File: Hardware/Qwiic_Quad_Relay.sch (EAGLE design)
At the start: 69 parts, among them J2 Qwiic Right Angle, J3 Qwiic Right Angle, J4 POWER_JACK, J9 AVR_SPI_PROG_3X2TESTPOINTS, K1 RELAY-SPDT-JZC-11F, K2 RELAY-SPDT-JZC-11F, K3 RELAY-SPDT-JZC-11F, K4 RELAY-SPDT-JZC-11F, Q1 600mA/40V, Q2 600mA/40V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

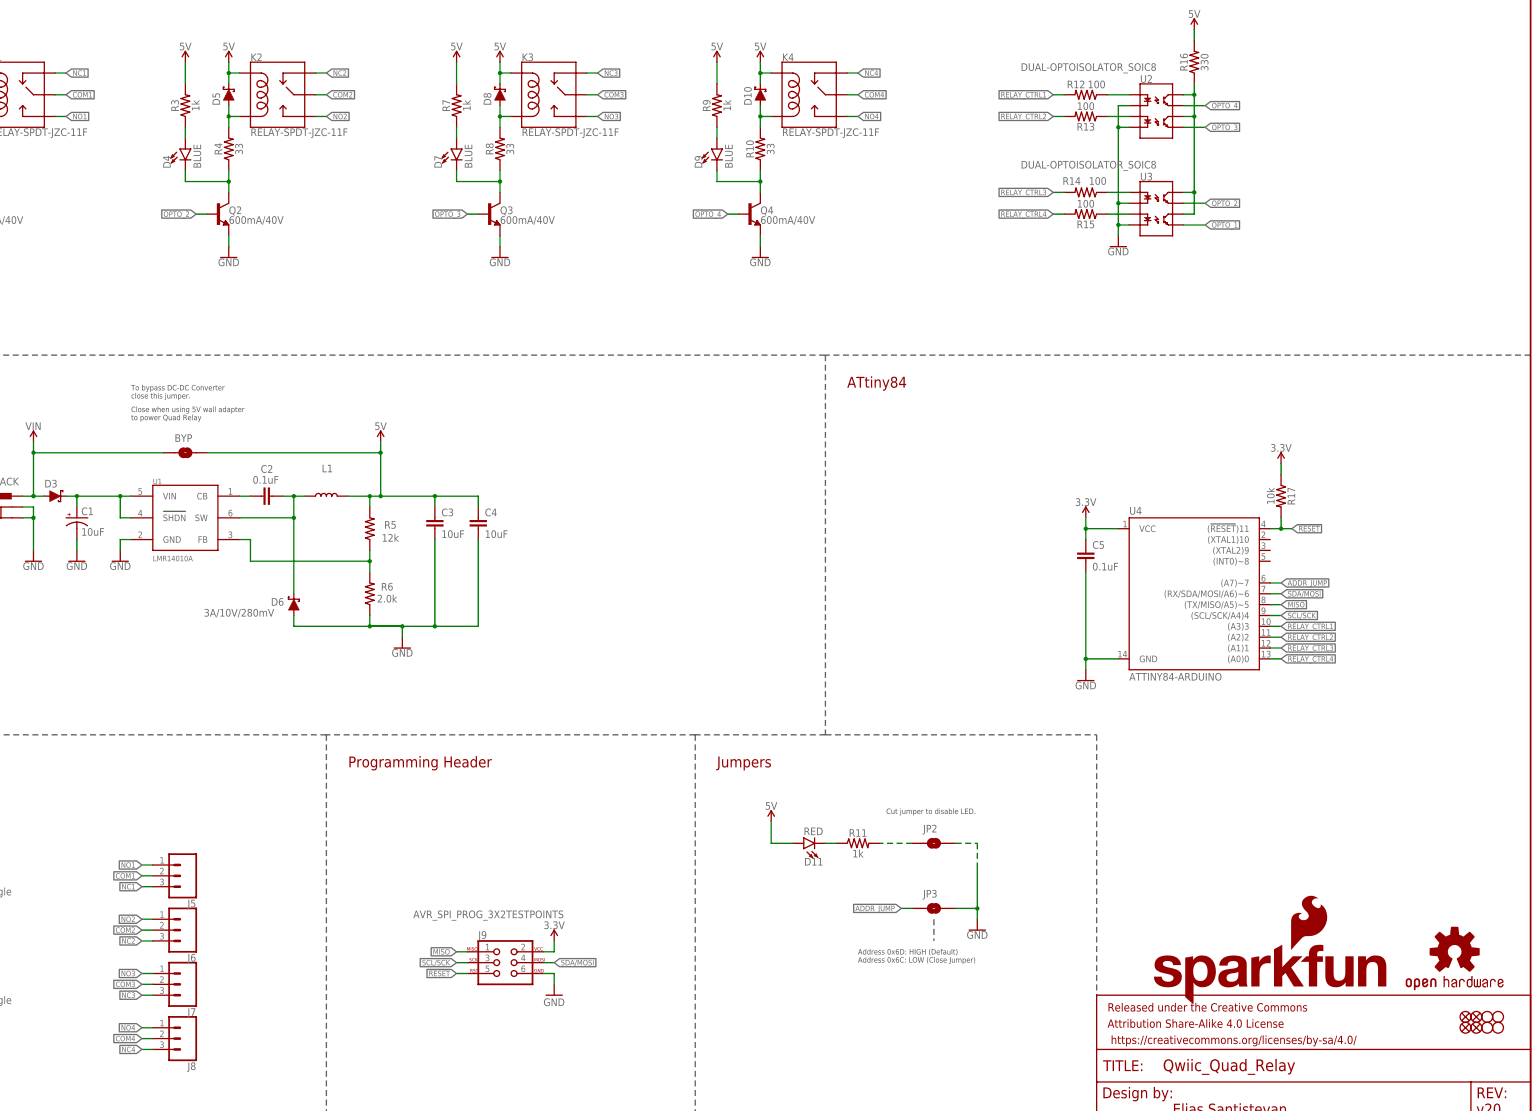
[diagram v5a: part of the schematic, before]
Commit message: Adds better silk, additional standoff, schotkky diode to protect dc/dc converter circuit
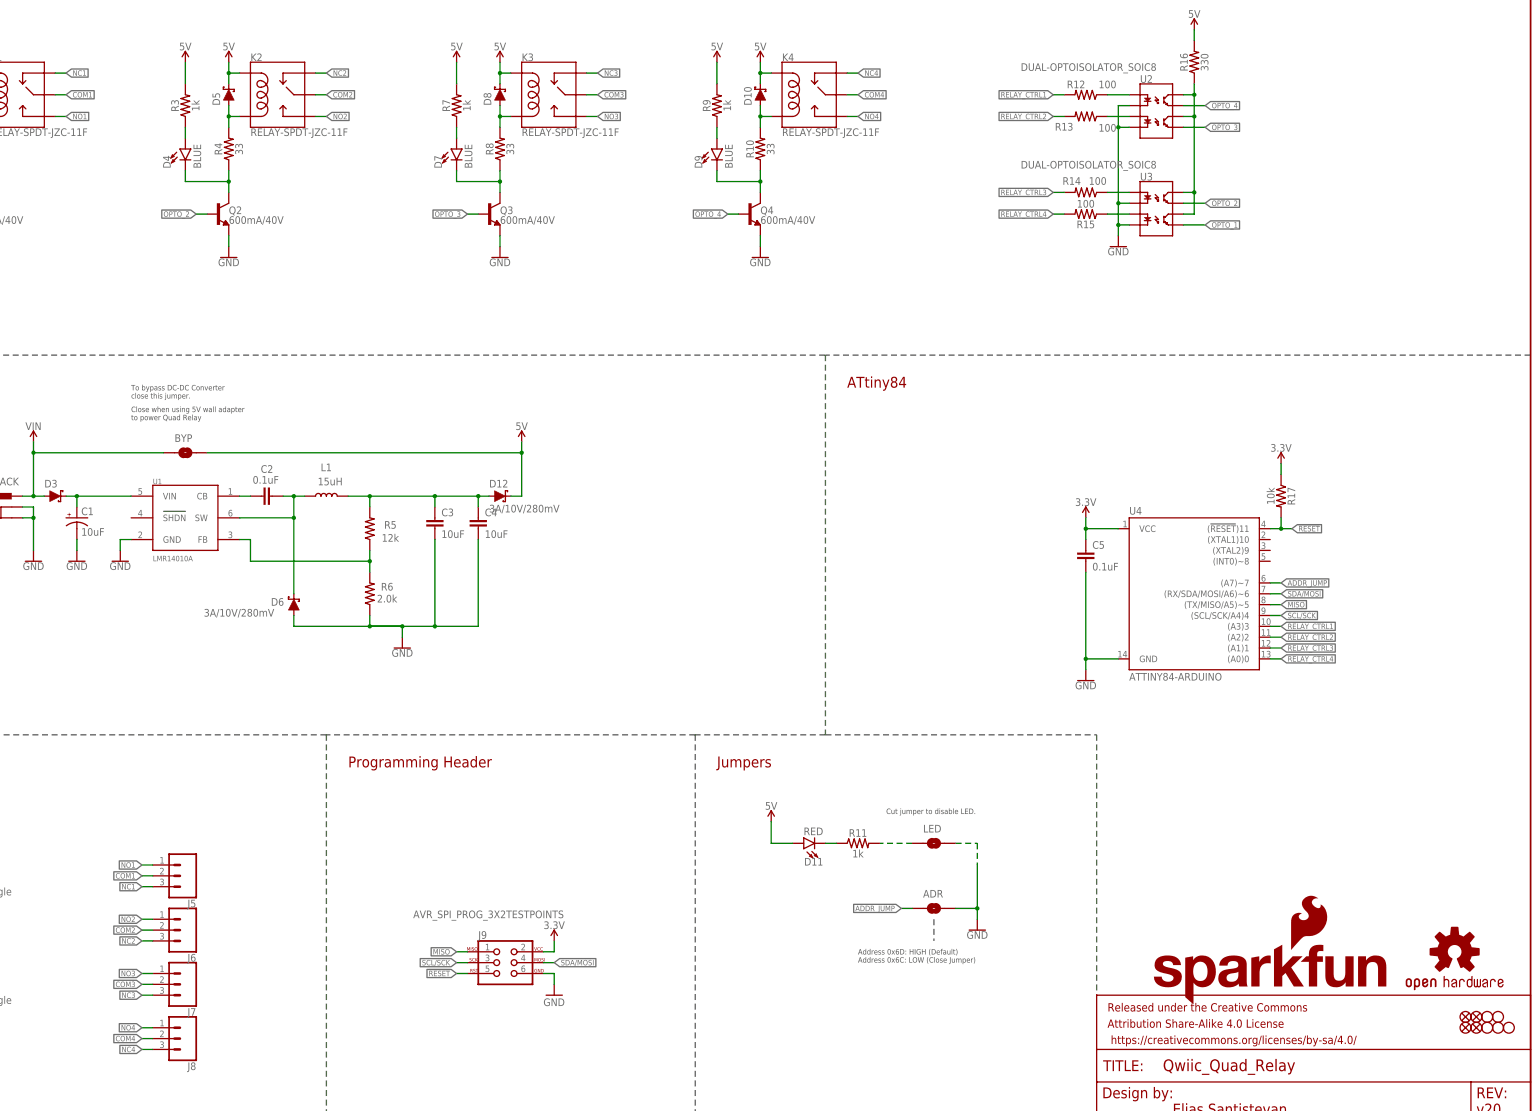
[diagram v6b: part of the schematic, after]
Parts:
- added D12: 3A/10V/280mV, SparkFun-DiscreteSemi:DIODE-SCHOTTKY-BAT60A
- added JP1: STAND-OFF, SparkFun-Hardware:STAND-OFF
- renumbered JP2 to LED, JP3 to ADR
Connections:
- new net 5V_OUT: C3.1, C4.1, D12.A, L1.2, R5.2
- net 5V: now also D12.C; no longer C3.1, C4.1, L1.2, R5.2
- net VIN_DC_DC: no longer U1.SHDN
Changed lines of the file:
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@@
 <part name="J4" library="SparkFun-Connectors" deviceset="POWER_JACK" device=""/>
 <part name="GND13" library="SparkFun-PowerSymbols" deviceset="GND" device=""/>
-<part name="SUPPLY16" library="SparkFun-PowerSymbols" deviceset="5V" device=""/>
 <part name="SUPPLY17" library="SparkFun-PowerSymbols" deviceset="3.3V" device=""/>
 <part name="LOGO2" library="SparkFun-Aesthetics" deviceset="OSHW-LOGO" device="S" value="OSHW-LOGOS"/>
@@
 <part name="SUPPLY19" library="SparkFun-PowerSymbols" deviceset="VIN" device=""/>
 <part name="GND18" library="SparkFun-PowerSymbols" deviceset="GND" device=""/>
-<part name="JP3" library="SparkFun-Jumpers" deviceset="JUMPER-SMT_2_NO" device="_SILK" package3d_urn="urn:adsk.eagle:package:39279/1"/>
+<part name="ADR" library="SparkFun-Jumpers" deviceset="JUMPER-SMT_2_NO" device="_SILK" package3d_urn="urn:adsk.eagle:package:39279/1"/>
 <part name="LOGO1" library="SparkFun-Aesthetics" deviceset="SFE_LOGO_NAME_FLAME" device=".1_INCH"/>
 <part name="U1" library="SparkFun-IC-Power" deviceset="LMR14010A" device=""/>
@@
 <part name="R5" library="SparkFun-Resistors" deviceset="12KOHM" device="-0603-1/10W-1%" value="12k"/>
 <part name="D6" library="SparkFun-DiscreteSemi" deviceset="DIODE-SCHOTTKY" device="-BAT60A" value="3A/10V/280mV"/>
-<part name="JP2" library="SparkFun-Jumpers" deviceset="JUMPER-SMT_2_NO" device="_SILK" package3d_urn="urn:adsk.eagle:package:39279/1"/>
+<part name="LED" library="SparkFun-Jumpers" deviceset="JUMPER-SMT_2_NO" device="_SILK" package3d_urn="urn:adsk.eagle:package:39279/1"/>
 <part name="BYP" library="SparkFun-Jumpers" deviceset="JUMPER-SMT_2_NO" device="_SILK" package3d_urn="urn:adsk.eagle:package:39279/1"/>
 <part name="GND7" library="SparkFun-PowerSymbols" deviceset="GND" device=""/>
+<part name="JP1" library="SparkFun-Hardware" deviceset="STAND-OFF" device=""/>
+<part name="D12" library="SparkFun-DiscreteSemi" deviceset="DIODE-SCHOTTKY" device="-BAT60A" value="3A/10V/280mV"/>
+<part name="SUPPLY7" library="SparkFun-PowerSymbols" deviceset="5V" device=""/>
 </parts>
 <sheets>
@@
 <instance part="R12" gate="G$1" x="586.74" y="246.38" smashed="yes" rot="R180">
 <attribute name="NAME" x="584.454" y="249.682" size="1.778" layer="95" font="vector" rot="R180" align="bottom-center"/>
-<attribute name="VALUE" x="589.28" y="247.904" size="1.778" layer="96" font="vector" rot="R180" align="top-center"/>
+<attribute name="VALUE" x="591.82" y="247.904" size="1.778" layer="96" font="vector" rot="R180" align="top-center"/>
 </instance>
 <instance part="R13" gate="G$1" x="586.74" y="241.3" smashed="yes" rot="R180">
-<attribute name="NAME" x="586.74" y="239.776" size="1.778" layer="95" font="vector" rot="R180" align="bottom-center"/>
-<attribute name="VALUE" x="586.74" y="242.824" size="1.778" layer="96" font="vector" rot="R180" align="top-center"/>
+<attribute name="NAME" x="581.66" y="239.776" size="1.778" layer="95" font="vector" rot="R180" align="bottom-center"/>
+<attribute name="VALUE" x="591.82" y="237.744" size="1.778" layer="96" font="vector" rot="R180" align="top-center"/>
 </instance>
 <instance part="R14" gate="G$1" x="586.74" y="223.52" smashed="yes" rot="R180">
@@
 <instance part="GND13" gate="1" x="340.36" y="137.16" smashed="yes">
 <attribute name="VALUE" x="340.36" y="136.906" size="1.778" layer="96" align="top-center"/>
-</instance>
-<instance part="SUPPLY16" gate="G$1" x="421.64" y="165.1" smashed="yes">
-<attribute name="VALUE" x="421.64" y="167.894" size="1.778" layer="96" align="bottom-center"/>
 </instance>
 <instance part="SUPPLY17" gate="G$1" x="462.28" y="48.26" smashed="yes">
@@
 <attribute name="VALUE" x="561.34" y="50.546" size="1.778" layer="96" align="top-center"/>
 </instance>
-<instance part="JP3" gate="G$1" x="551.18" y="55.88" smashed="yes">
+<instance part="ADR" gate="G$1" x="551.18" y="55.88" smashed="yes">
 <attribute name="NAME" x="548.64" y="58.42" size="1.778" layer="95" font="vector"/>
 </instance>
@@
 </instance>
 <instance part="L1" gate="G$1" x="408.94" y="152.4" smashed="yes" rot="R90">
-<attribute name="NAME" x="410.464" y="159.766" size="1.778" layer="95" font="vector" rot="R180"/>
+<attribute name="NAME" x="410.21" y="160.02" size="1.778" layer="95" font="vector" rot="R180"/>
+<attribute name="VALUE" x="412.75" y="154.94" size="1.778" layer="96" font="vector" rot="R180" align="top-left"/>
 </instance>
 <instance part="R6" gate="G$1" x="419.1" y="129.54" smashed="yes" rot="R90">
@@
 <attribute name="VALUE" x="380.238" y="125.984" size="1.778" layer="96" font="vector" align="top-left"/>
 </instance>
-<instance part="JP2" gate="G$1" x="551.18" y="71.12" smashed="yes" rot="R180">
+<instance part="LED" gate="G$1" x="551.18" y="71.12" smashed="yes" rot="R180">
 <attribute name="NAME" x="548.64" y="73.66" size="1.778" layer="95" font="vector"/>
 </instance>
@@
 <instance part="GND7" gate="1" x="462.28" y="35.56" smashed="yes">
 <attribute name="VALUE" x="459.74" y="33.02" size="1.778" layer="96"/>
+</instance>
+<instance part="JP1" gate="G$1" x="685.8" y="27.94" smashed="yes"/>
+<instance part="D12" gate="G$1" x="449.58" y="152.4" smashed="yes">
+<attribute name="NAME" x="447.04" y="154.432" size="1.778" layer="95" font="vector"/>
+<attribute name="VALUE" x="447.04" y="150.368" size="1.778" layer="96" font="vector" align="top-left"/>
+</instance>
+<instance part="SUPPLY7" gate="G$1" x="454.66" y="165.1" smashed="yes">
+<attribute name="VALUE" x="454.66" y="167.894" size="1.778" layer="96" align="bottom-center"/>
 </instance>
 </instances>
@@
 <wire x1="556.26" y1="55.88" x2="561.34" y2="55.88" width="0.1524" layer="91"/>
 <wire x1="561.34" y1="55.88" x2="561.34" y2="53.34" width="0.1524" layer="91"/>
-<pinref part="JP3" gate="G$1" pin="2"/>
-<pinref part="JP2" gate="G$1" pin="1"/>
+<pinref part="ADR" gate="G$1" pin="2"/>
+<pinref part="LED" gate="G$1" pin="1"/>
 <wire x1="556.26" y1="71.12" x2="561.34" y2="71.12" width="0.1524" layer="91" style="longdash"/>
 <wire x1="561.34" y1="71.12" x2="561.34" y2="66.04" width="0.1524" layer="91" style="longdash"/>
@@
 </segment>
 <segment>
+<pinref part="D12" gate="G$1" pin="C"/>
+<wire x1="452.12" y1="152.4" x2="454.66" y2="152.4" width="0.1524" layer="91"/>
+<wire x1="454.66" y1="152.4" x2="454.66" y2="162.56" width="0.1524" layer="91"/>
+<pinref part="SUPPLY7" gate="G$1" pin="5V"/>
 <pinref part="BYP" gate="G$1" pin="2"/>
-<pinref part="L1" gate="G$1" pin="2"/>
-<pinref part="C3" gate="G$1" pin="1"/>
-<wire x1="414.02" y1="152.4" x2="419.1" y2="152.4" width="0.1524" layer="91"/>
-<wire x1="419.1" y1="152.4" x2="421.64" y2="152.4" width="0.1524" layer="91"/>
-<wire x1="421.64" y1="152.4" x2="434.34" y2="152.4" width="0.1524" layer="91"/>
-<wire x1="434.34" y1="152.4" x2="434.34" y2="149.86" width="0.1524" layer="91"/>
-<wire x1="434.34" y1="152.4" x2="444.5" y2="152.4" width="0.1524" layer="91"/>
-<junction x="434.34" y="152.4"/>
-<pinref part="C4" gate="G$1" pin="1"/>
-<wire x1="444.5" y1="152.4" x2="444.5" y2="149.86" width="0.1524" layer="91"/>
-<pinref part="SUPPLY16" gate="G$1" pin="5V"/>
-<pinref part="R5" gate="G$1" pin="2"/>
-<wire x1="419.1" y1="152.4" x2="419.1" y2="149.86" width="0.1524" layer="91"/>
-<junction x="419.1" y="152.4"/>
-<wire x1="421.64" y1="152.4" x2="421.64" y2="162.56" width="0.1524" layer="91"/>
-<junction x="421.64" y="152.4"/>
-<wire x1="421.64" y1="162.56" x2="421.64" y2="165.1" width="0.1524" layer="91"/>
-<wire x1="381" y1="162.56" x2="421.64" y2="162.56" width="0.1524" layer="91"/>
-<junction x="421.64" y="162.56"/>
+<wire x1="454.66" y1="162.56" x2="454.66" y2="165.1" width="0.1524" layer="91"/>
+<wire x1="381" y1="162.56" x2="454.66" y2="162.56" width="0.1524" layer="91"/>
+<junction x="454.66" y="162.56"/>
 </segment>
 </net>
@@
 <wire x1="347.98" y1="152.4" x2="350.52" y2="152.4" width="0.1524" layer="91"/>
 <pinref part="U1" gate="G$1" pin="VIN"/>
-<wire x1="363.22" y1="152.4" x2="360.68" y2="152.4" width="0.1524" layer="91"/>
-<pinref part="U1" gate="G$1" pin="SHDN"/>
-<wire x1="360.68" y1="152.4" x2="350.52" y2="152.4" width="0.1524" layer="91"/>
-<wire x1="363.22" y1="147.32" x2="360.68" y2="147.32" width="0.1524" layer="91"/>
-<wire x1="360.68" y1="147.32" x2="360.68" y2="152.4" width="0.1524" layer="91"/>
-<junction x="360.68" y="152.4"/>
+<wire x1="363.22" y1="152.4" x2="350.52" y2="152.4" width="0.1524" layer="91"/>
 </segment>
 </net>
@@
 </segment>
 <segment>
-<pinref part="JP3" gate="G$1" pin="1"/>
+<pinref part="ADR" gate="G$1" pin="1"/>
 <wire x1="546.1" y1="55.88" x2="543.56" y2="55.88" width="0.1524" layer="91"/>
 <label x="543.56" y="55.88" size="1.27" layer="95" rot="R180" xref="yes"/>
@@
 <net name="N$14" class="0">
 <segment>
-<pinref part="JP2" gate="G$1" pin="2"/>
+<pinref part="LED" gate="G$1" pin="2"/>
 <pinref part="R11" gate="G$1" pin="2"/>
 <wire x1="546.1" y1="71.12" x2="538.48" y2="71.12" width="0.1524" layer="91" style="longdash"/>
@@
 </segment>
 </net>
+<net name="5V_OUT" class="0">
+<segment>
+<pinref part="L1" gate="G$1" pin="2"/>
+<pinref part="C3" gate="G$1" pin="1"/>
+<wire x1="414.02" y1="152.4" x2="419.1" y2="152.4" width="0.1524" layer="91"/>
+<wire x1="419.1" y1="152.4" x2="434.34" y2="152.4" width="0.1524" layer="91"/>
+<wire x1="434.34" y1="152.4" x2="434.34" y2="149.86" width="0.1524" layer="91"/>
+<wire x1="434.34" y1="152.4" x2="444.5" y2="152.4" width="0.1524" layer="91"/>
+<junction x="434.34" y="152.4"/>
+<pinref part="C4" gate="G$1" pin="1"/>
+<wire x1="444.5" y1="152.4" x2="444.5" y2="149.86" width="0.1524" layer="91"/>
+<pinref part="R5" gate="G$1" pin="2"/>
+<wire x1="419.1" y1="152.4" x2="419.1" y2="149.86" width="0.1524" layer="91"/>
+<junction x="419.1" y="152.4"/>
+<pinref part="D12" gate="G$1" pin="A"/>
+<wire x1="447.04" y1="152.4" x2="444.5" y2="152.4" width="0.1524" layer="91"/>
+<junction x="444.5" y="152.4"/>
+</segment>
+</net>

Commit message: Fixes inductor
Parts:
- L1: device SparkFun-Coils:INDUCTOR-DEM-2818C-15UH -> SparkFun-Coils:INDUCTOR-LQH5B-15UH
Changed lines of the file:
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@@
 <part name="GND20" library="SparkFun-PowerSymbols" deviceset="GND" device=""/>
 <part name="C2" library="SparkFun-Capacitors" deviceset="0.1UF" device="-0402-10V-10%-X7R" value="0.1uF"/>
-<part name="L1" library="SparkFun-Coils" deviceset="INDUCTOR" device="-DEM-2818C-15UH" value="15uH"/>
+<part name="L1" library="SparkFun-Coils" deviceset="INDUCTOR" device="-LQH5B-15UH" value="15uH"/>
 <part name="R6" library="SparkFun-Resistors" deviceset="2.0KOHM" device="-0603-1/10W-5%" value="2.0k"/>
 <part name="R5" library="SparkFun-Resistors" deviceset="12KOHM" device="-0603-1/10W-1%" value="12k"/>

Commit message: Adds silk to indicate qwiic board standoffs
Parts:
- J1: device SparkFun-Connectors:CONN_041X04_NO_SILK -> SparkFun-Connectors:CONN_041X04_NO_SILK_NO_POP
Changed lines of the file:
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@@
 <part name="FD4" library="SparkFun-Aesthetics" deviceset="FIDUCIAL" device="1X2"/>
 <part name="GND8" library="SparkFun-PowerSymbols" deviceset="GND" device=""/>
-<part name="J1" library="SparkFun-Connectors" deviceset="CONN_04" device="1X04_NO_SILK"/>
+<part name="J1" library="SparkFun-Connectors" deviceset="CONN_04" device="1X04_NO_SILK_NO_POP"/>
 <part name="U3" library="SparkFun-DiscreteSemi" deviceset="DUAL-OPTOISOLATOR" device="_SOIC8"/>
 <part name="U2" library="SparkFun-DiscreteSemi" deviceset="DUAL-OPTOISOLATOR" device="_SOIC8"/>
